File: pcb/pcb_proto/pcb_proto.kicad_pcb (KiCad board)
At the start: 2 copper layers, 67.3 x 43.2 mm, 18 parts, among them J1 Conn_01x02, J3 CONSOLE, SW1 MODE, SW2 UP, SW3 DOWN, U1 ATmega328P-PU, U2 MPXV5010, U3 LTC-4627, Y1 Resonator_Small

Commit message: update through hole board
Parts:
- J1: value Conn_01x02 -> Barrel_Jack; footprint Connector_JST:JST_EH_B2B-EH-A_1x02_P2.50mm_Vertical -> Connector_BarrelJack:BarrelJack_Wuerth_6941xx301002
- SW1: value MODE -> SW_Push; footprint common:PTS636 SK43 LFS -> common:SW_PUSH_6mm
- SW2: value UP -> SW_Push; footprint common:PTS636 SK43 LFS -> common:SW_PUSH_6mm
- SW3: value DOWN -> SW_Push; footprint common:PTS636 SK43 LFS -> common:SW_PUSH_6mm
- moved SW1 161.9 mm to (7.62, -6.35), turned to 0 degrees
- moved SW2 159.1 mm to (22.9, -6.35), turned to 0 degrees
- moved SW3 156.8 mm to (37.5, -6.35), turned to 0 degrees
- moved J1 156.8 mm to (54.6, -11.4), turned to 0 degrees
- moved BZ1 153.2 mm to (14.6, -16.5)
- moved C4 152.7 mm to (20.3, -19.0)
- moved C1 152.7 mm to (41.9, -14.0)
- moved C2 152.7 mm to (36.8, -14.0)
- moved C5 152.7 mm to (20.3, -25.4)
- moved ISP1 152.7 mm to (44.5, -22.9)
- moved RN1 152.7 mm to (21.6, -29.2)
- moved RN2 152.7 mm to (36.8, -29.2)
- moved U1 152.7 mm to (24.1, -17.8)
- moved U2 152.7 mm to (8.89, -26.7)
- moved U3 152.7 mm to (39.4, -38.1)
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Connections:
- J1 pad 1: GND -> +5V
- J1 pad 2: +5V -> GND
- SW1 pad 1: Net-(SW1-Pad1) -> (no net)
- SW2 pad 4: GND -> (no net)
- SW3 pad 4: GND -> (no net)
- U1 pad 2: Net-(BZ1-Pad1) -> Net-(SW1-Pad1)
- U1 pad 4: Net-(SW1-Pad1) -> Net-(SW2-Pad1)
- U1 pad 5: Net-(SW2-Pad1) -> Net-(BZ1-Pad1)
- U3 pad 16: (no net) -> /MISO
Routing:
- net Net-(BZ1-Pad1): track 13.0 -> 45.4 mm
- net /MISO: track 8.58 -> 36.5 mm
- net Net-(J3-Pad1): track 26.5 -> 8.15 mm
- net +5V: track 108.8 -> 117.3 mm
- net GND: track 0.00 -> 7.84 mm
- net Net-(SW3-Pad1): track 20.0 -> 17.2 mm
- net (no net): track 0.00 -> 2.54 mm, vias 2 -> 4
- net Net-(SW2-Pad1): track 15.7 -> 17.5 mm
- net /RST: track 35.8 -> 34.3 mm
- net /f: track 35.2 -> 36.3 mm
- net /c: track 40.0 -> 40.8 mm
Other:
- board size 67.3 x 43.2 mm -> 67.3 x 44.5 mm

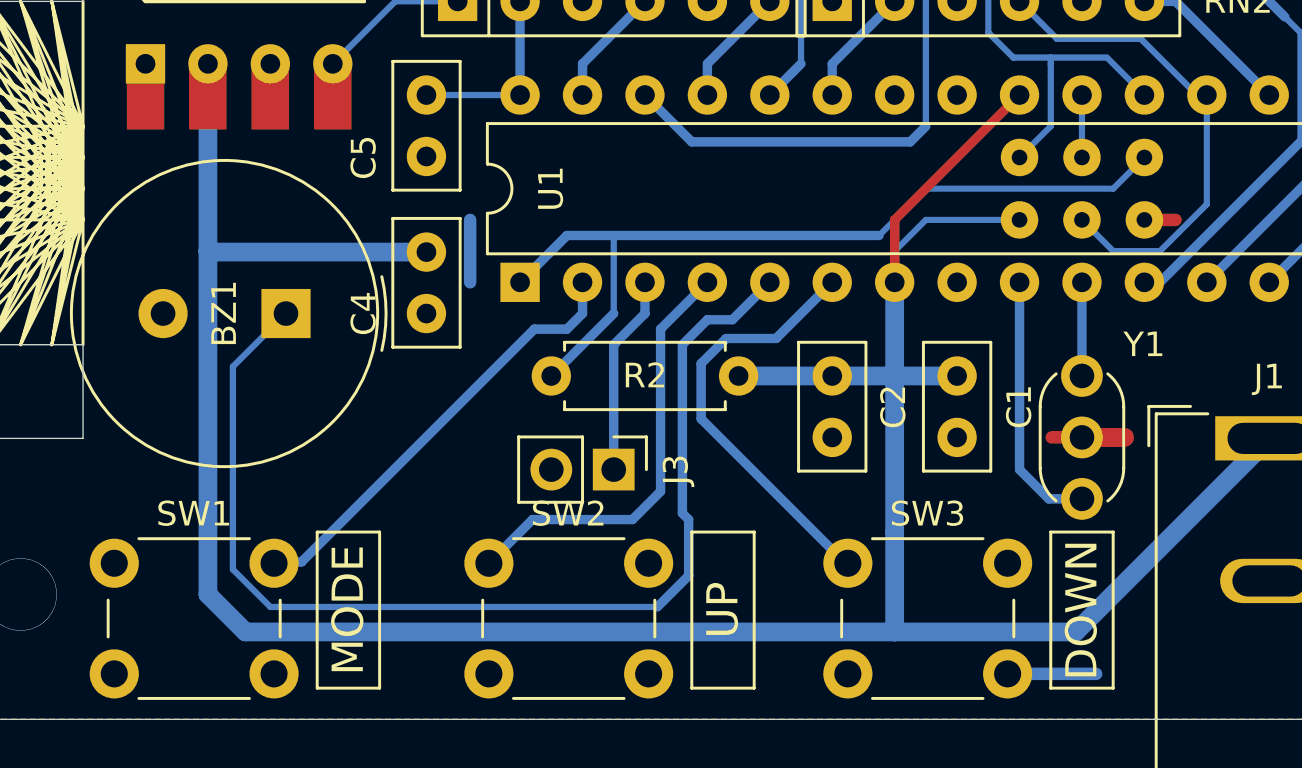
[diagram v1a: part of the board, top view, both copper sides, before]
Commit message: remove gerbers
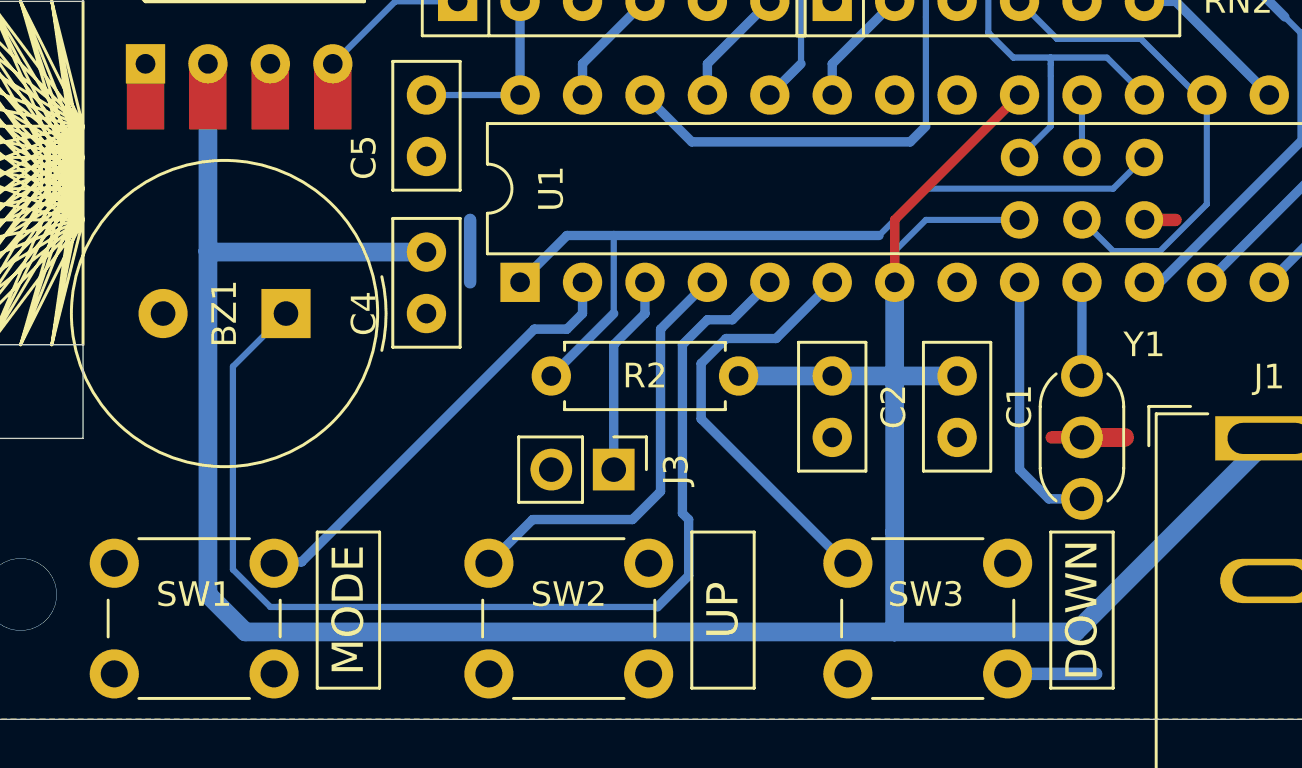
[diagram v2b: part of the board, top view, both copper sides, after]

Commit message: button order
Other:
- board text added: "Evan Widloski 2020-04-07 RapidAlarm v1"
- board text removed: "Evan Widloski 2020-04-07 Ventmon v1"
